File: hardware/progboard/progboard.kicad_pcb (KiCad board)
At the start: 2 copper layers, 74.9 x 58.4 mm, 37 parts, among them J1 LEFT, J2 RIGHT, J3 SWD, J4 CV A, J5 POWER

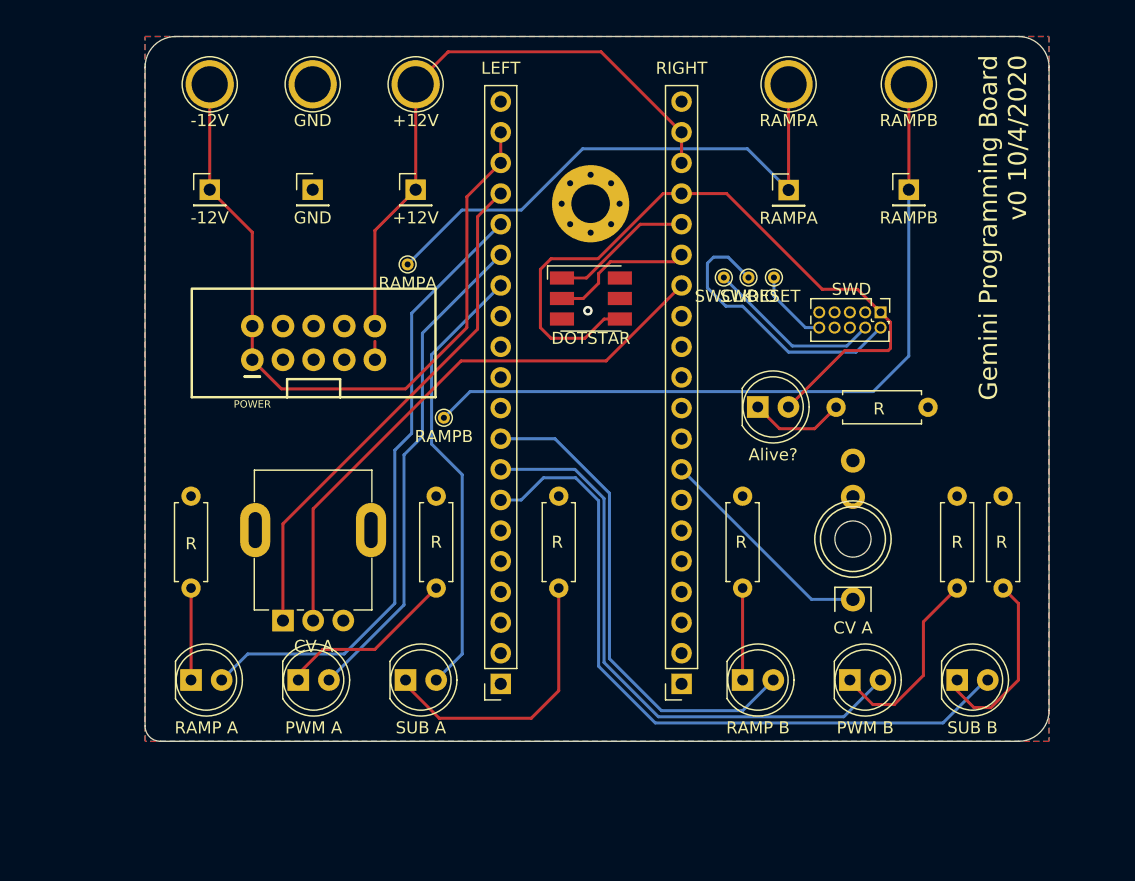
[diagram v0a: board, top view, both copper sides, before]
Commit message: Adjust drill sizes for pogo pins
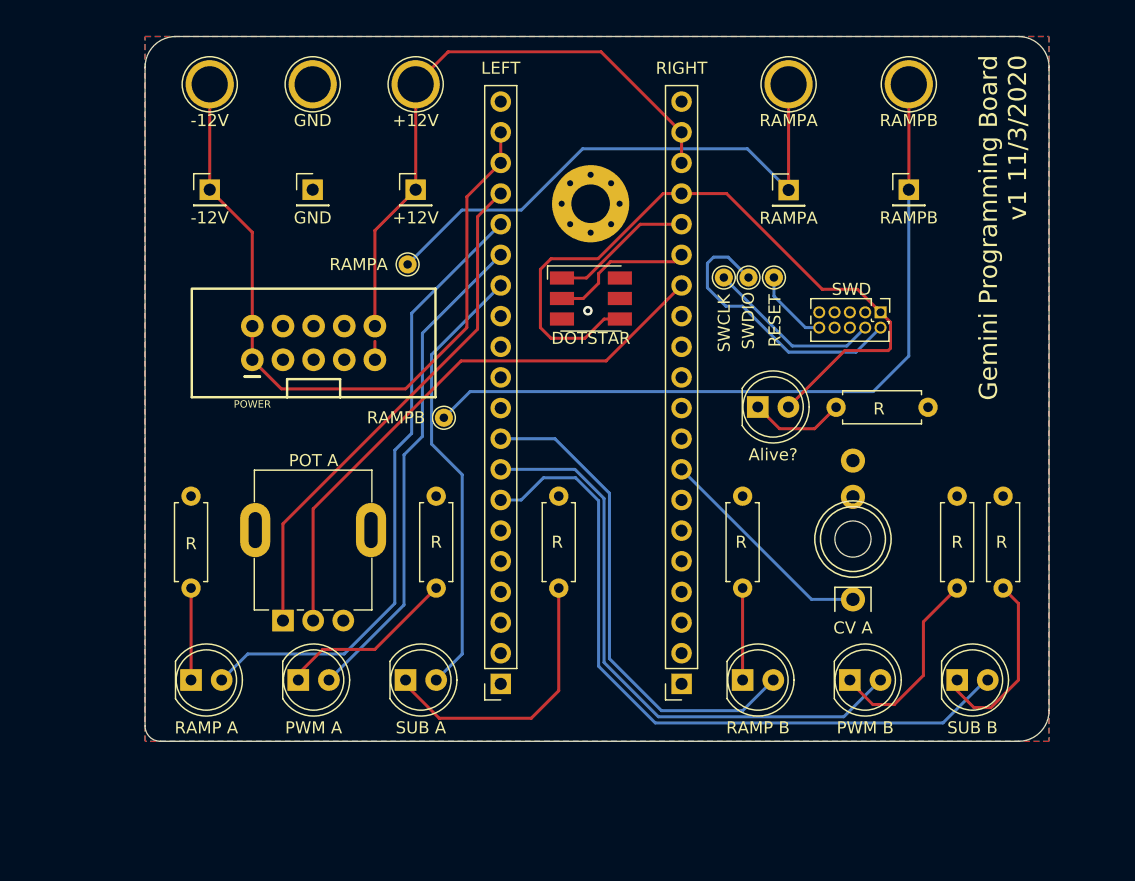
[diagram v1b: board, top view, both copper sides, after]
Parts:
- RV1: value CV A -> POT A
- TP1, TP2, TP3, TP4, TP5: footprint TestPoint:TestPoint_THTPad_D1.0mm_Drill0.5mm -> TestPoint:TestPoint_THTPad_D1.5mm_Drill0.7mm
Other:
- board text added: "Gemini Programming Board v1 11/3/2020"
- board text removed: "Gemini Programming Board v0 10/4/2020"

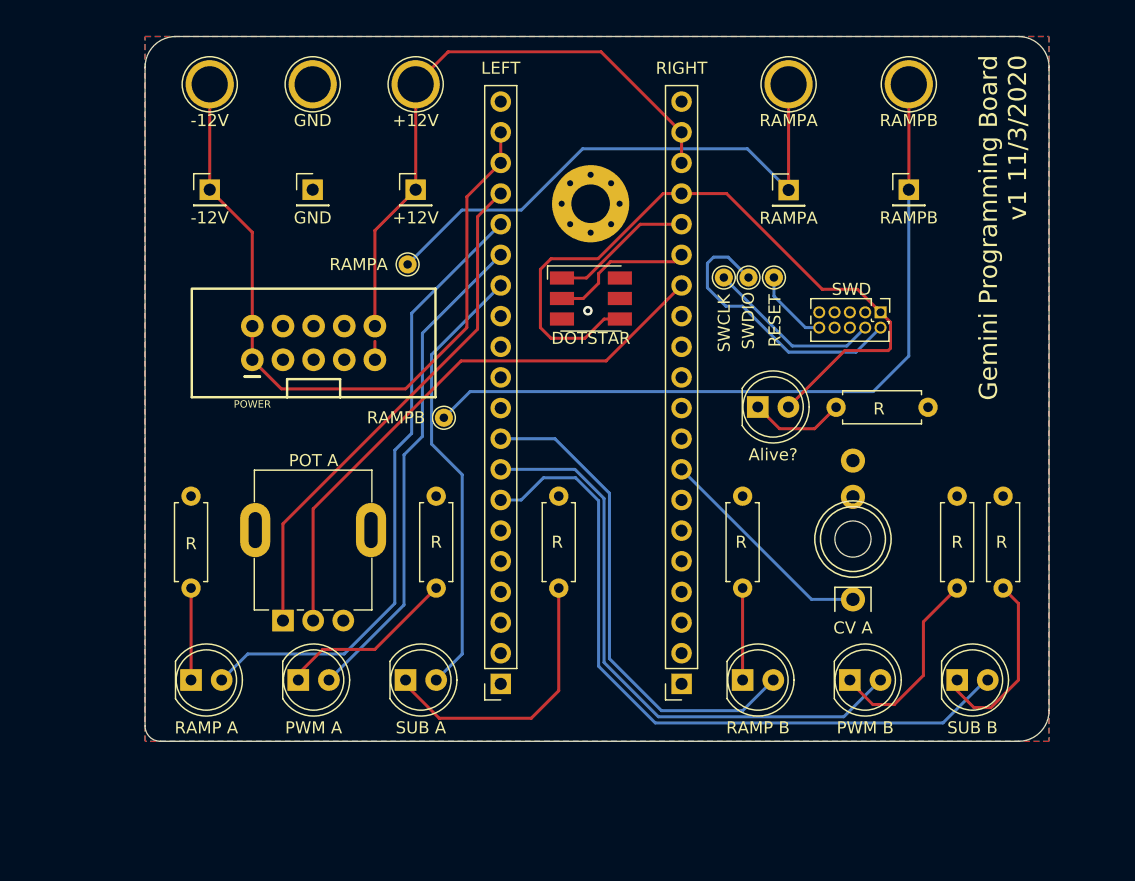
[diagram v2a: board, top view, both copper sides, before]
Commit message: hardware: new revision of programming board with more comprehensive test points
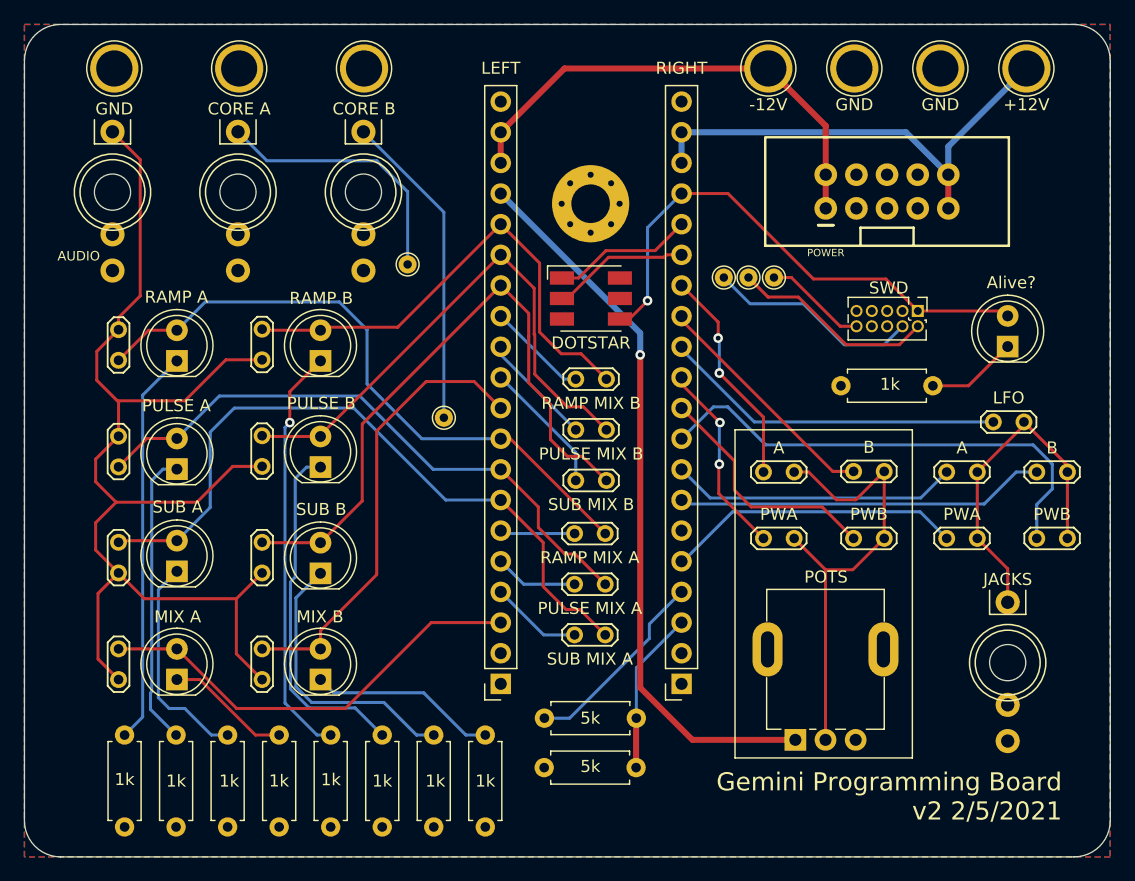
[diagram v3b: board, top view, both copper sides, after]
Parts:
- removed TP11: -12V, Connector_PinHeader_2.54mm:PinHeader_1x01_P2.54mm_Vertical
- removed TP12: GND, Connector_PinHeader_2.54mm:PinHeader_1x01_P2.54mm_Vertical
- removed TP13: +12V, Connector_PinHeader_2.54mm:PinHeader_1x01_P2.54mm_Vertical
- removed TP14: RAMPA, Connector_PinHeader_2.54mm:PinHeader_1x01_P2.54mm_Vertical
- removed TP15: RAMPB, Connector_PinHeader_2.54mm:PinHeader_1x01_P2.54mm_Vertical
- added D10: MIX B, LED_THT:LED_D5.0mm, F.Cu at (130.1, 115.5)
- added D9: MIX A, LED_THT:LED_D5.0mm, F.Cu at (118.2, 115.5)
- added J6: AUDIO, progboard:WQP-PJ301M-12_JACK, F.Cu at (112.9, 75.1)
- added J7: CORE A, progboard:WQP-PJ301M-12_JACK, F.Cu at (123.3, 75.1)
- added J8: CORE B, progboard:WQP-PJ301M-12_JACK, F.Cu at (133.7, 75.1)
- added JP1: RAMP MIX A, TestPoint:TestPoint_2Pads_Pitch2.54mm_Drill0.8mm, F.Cu at (151.2, 103.4)
- added JP10: PWB, TestPoint:TestPoint_2Pads_Pitch2.54mm_Drill0.8mm, F.Cu at (176.8, 103.8)
- added JP11: RAMP A, TestPoint:TestPoint_2Pads_Pitch2.54mm_Drill0.8mm, F.Cu at (113.4, 86.5)
- added JP12: PULSE A, TestPoint:TestPoint_2Pads_Pitch2.54mm_Drill0.8mm, F.Cu at (113.4, 95.4)
- added JP13: SUB A, TestPoint:TestPoint_2Pads_Pitch2.54mm_Drill0.8mm, F.Cu at (113.4, 106.7)
- added JP14: MIX A, TestPoint:TestPoint_2Pads_Pitch2.54mm_Drill0.8mm, F.Cu at (113.4, 115.5)
- added JP15: RAMP B, TestPoint:TestPoint_2Pads_Pitch2.54mm_Drill0.8mm, F.Cu at (125.3, 89.0)
- added JP16: PULSE B, TestPoint:TestPoint_2Pads_Pitch2.54mm_Drill0.8mm, F.Cu at (125.3, 97.9)
- added JP17: SUB B, TestPoint:TestPoint_2Pads_Pitch2.54mm_Drill0.8mm, F.Cu at (125.3, 106.7)
- added JP18: MIX B, TestPoint:TestPoint_2Pads_Pitch2.54mm_Drill0.8mm, F.Cu at (125.3, 115.5)
- added JP19: A, TestPoint:TestPoint_2Pads_Pitch2.54mm_Drill0.8mm, F.Cu at (184.6, 98.3)
- added JP2: PULSE MIX A, TestPoint:TestPoint_2Pads_Pitch2.54mm_Drill0.8mm, F.Cu at (151.2, 107.6)
- added JP20: B, TestPoint:TestPoint_2Pads_Pitch2.54mm_Drill0.8mm, F.Cu at (192.0, 98.3)
- added JP21: PWA, TestPoint:TestPoint_2Pads_Pitch2.54mm_Drill0.8mm, F.Cu at (184.6, 103.8)
- added JP22: PWB, TestPoint:TestPoint_2Pads_Pitch2.54mm_Drill0.8mm, F.Cu at (192.0, 103.8)
- added JP23: LFO, TestPoint:TestPoint_2Pads_Pitch2.54mm_Drill0.8mm, F.Cu at (188.4, 94.2)
- added JP3: SUB MIX A, TestPoint:TestPoint_2Pads_Pitch2.54mm_Drill0.8mm, F.Cu at (151.2, 111.8)
- added JP4: RAMP MIX B, TestPoint:TestPoint_2Pads_Pitch2.54mm_Drill0.8mm, F.Cu at (151.3, 90.6)
- added JP5: PULSE MIX B, TestPoint:TestPoint_2Pads_Pitch2.54mm_Drill0.8mm, F.Cu at (151.3, 94.8)
- added JP6: SUB MIX B, TestPoint:TestPoint_2Pads_Pitch2.54mm_Drill0.8mm, F.Cu at (151.3, 99.0)
- added JP7: A, TestPoint:TestPoint_2Pads_Pitch2.54mm_Drill0.8mm, F.Cu at (169.4, 98.3)
- added JP8: B, TestPoint:TestPoint_2Pads_Pitch2.54mm_Drill0.8mm, F.Cu at (176.8, 98.3)
- added JP9: PWA, TestPoint:TestPoint_2Pads_Pitch2.54mm_Drill0.8mm, F.Cu at (169.4, 103.8)
- added R1: 5k, Resistor_THT:R_Axial_DIN0207_L6.3mm_D2.5mm_P7.62mm_Horizontal, F.Cu at (148.7, 118.7)
- added R11: 1k, Resistor_THT:R_Axial_DIN0207_L6.3mm_D2.5mm_P7.62mm_Horizontal, F.Cu at (143.8, 120.1)
- added R2: 5k, Resistor_THT:R_Axial_DIN0207_L6.3mm_D2.5mm_P7.62mm_Horizontal, F.Cu at (156.3, 122.8)
- added R7: 1k, Resistor_THT:R_Axial_DIN0207_L6.3mm_D2.5mm_P7.62mm_Horizontal, F.Cu at (126.7, 120.1)
- added TP16: GND, TestPoint:TestPoint_Plated_Hole_D3.0mm, F.Cu at (113.0, 64.9)
- added TP17: GND, TestPoint:TestPoint_Plated_Hole_D3.0mm, F.Cu at (181.5, 64.9)
- D3: value PWM A -> PULSE A
- D6: value PWM B -> PULSE B
- J4: value CV A -> JACKS
- R10: renamed from 1k6; value R -> 1k
- R3: renamed from 1k7; value R -> 1k
- R4: renamed from 1k1; value R -> 1k
- R5: renamed from 1k2; value R -> 1k
- R6: renamed from 1k3; value R -> 1k
- R8: renamed from 1k4; value R -> 1k
- R9: renamed from 1k5; value R -> 1k
- RV1: value POT A -> POTS
- TP10, TP5: value RAMPB -> CORE B
- TP4, TP9: value RAMPA -> CORE A
- moved D7 53.5 mm to (130.1, 106.7), turned to 90 degrees
- moved TP8 50.6 mm to (188.6, 64.9)
- moved R9 49.2 mm to (135.2, 120.1), turned to 270 degrees
- moved J5 49.2 mm to (177.1, 75.1)
- moved R10 48.7 mm to (139.5, 120.1), turned to 270 degrees
- moved D6 47.3 mm to (130.1, 97.9), turned to 90 degrees
- moved TP6 46.3 mm to (167.2, 64.9)
- moved TP9 45.6 mm to (123.4, 64.9)
- moved TP10 45.2 mm to (133.7, 64.9)
- moved TP7 44.9 mm to (174.4, 64.9)
- moved D5 43.9 mm to (130.1, 89.1), turned to 90 degrees
- moved RV1 43.6 mm to (169.5, 120.5)
- moved R8 36.3 mm to (131.0, 120.1), turned to 270 degrees
- moved R6 30.0 mm to (122.4, 120.1), turned to 270 degrees
- moved D2 26.5 mm to (118.2, 89.1), turned to 90 degrees
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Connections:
- net Net-(J2-Pad2) renamed /mix_out
- net Net-(J2-Pad6) renamed /button
- D2 pad 2: /pollux_ramp -> /castor_ramp
- D3 pad 2: /pollux_pwm -> /castor_pwm
- D4 pad 2: /pollux_sub -> /castor_sub
- D5 pad 2: /castor_ramp -> /pollux_ramp
- D6 pad 2: /castor_pwm -> /pollux_pwm
- D7 pad 2: /castor_sub -> /pollux_sub
- J1 pad 10: Net-(J1-Pad10) -> /pollux_mix_out
- J1 pad 11: Net-(J1-Pad11) -> /pollux_sub_mix_in
- J1 pad 12: Net-(J1-Pad12) -> /pollux_pwm_mix_in
- J1 pad 13: Net-(J1-Pad13) -> /pollux_ramp_mix_in
- J1 pad 3: Net-(J1-Pad3) -> /castor_mix_out
- J1 pad 4: Net-(J1-Pad4) -> /castor_sub_mix_in
- J1 pad 5: Net-(J1-Pad5) -> /castor_pwm_mix_in
- J1 pad 6: Net-(J1-Pad6) -> /castor_ramp_mix_in
- J2 pad 10: Net-(J2-Pad10) -> /duty_b_pot
- J2 pad 11: Net-(J2-Pad11) -> /duty_a_pot
- J2 pad 12: Net-(J2-Pad12) -> /chorus_pot
- J2 pad 13: Net-(J2-Pad13) -> /cv_b_pot
- J2 pad 3: Net-(J2-Pad3) -> /mix_pot_in
- J2 pad 4: Net-(J2-Pad4) -> /mix_pot_out
- J2 pad 5: Net-(J2-Pad5) -> /duty_a_jack
- J2 pad 7: Net-(J2-Pad7) -> /cv_b_jack
- J2 pad 9: Net-(J2-Pad9) -> /duty_b_jack
- J4 pad T: /cv_a_jack -> Net-(J4-PadT)
- J5 pad 9: Net-(J5-Pad9) -> +12V
- RV1 pad 2: /cv_a_pot -> Net-(JP10-Pad1)
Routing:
- net Net-(J6-PadT): track 0.00 -> 101.0 mm
- net /duty_b_jack: track 0.00 -> 40.5 mm
- net Net-(JP10-Pad1): track 0.00 -> 38.7 mm
- net /pollux_mix_out: track 0.00 -> 37.7 mm
- net Net-(J8-PadT): track 63.2 -> 26.5 mm
- net /castor_mix_out: track 0.00 -> 36.7 mm
- net /cv_b_jack: track 0.00 -> 30.7 mm
- net /cv_a_pot: track 47.5 -> 18.3 mm, vias 0 -> 2
- net Net-(J4-PadT): track 0.00 -> 28.7 mm
- net /chorus_pot: track 0.00 -> 28.5 mm
- net Net-(D5-Pad1): track 7.62 -> 34.5 mm, vias 0 -> 1
- net Net-(D2-Pad1): track 7.62 -> 32.8 mm
- net /duty_a_jack: track 0.00 -> 24.6 mm
- net Net-(J7-PadT): track 45.7 -> 22.1 mm
- net -12V: track 62.5 -> 40.5 mm
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- added copper zone on B.Cu, net /pollux_sub
- removed copper zone on B.Cu, net GND
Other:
- board size 74.9 x 58.4 mm -> 90 x 69 mm
- board text added: "Gemini Programming Board v2 2/5/2021"
- board text removed: "Gemini Programming Board v1 11/3/2020"
- board text removed: "OwO"

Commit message: hardware/progboard: Add dedicated jack for interfacing with knob inputs
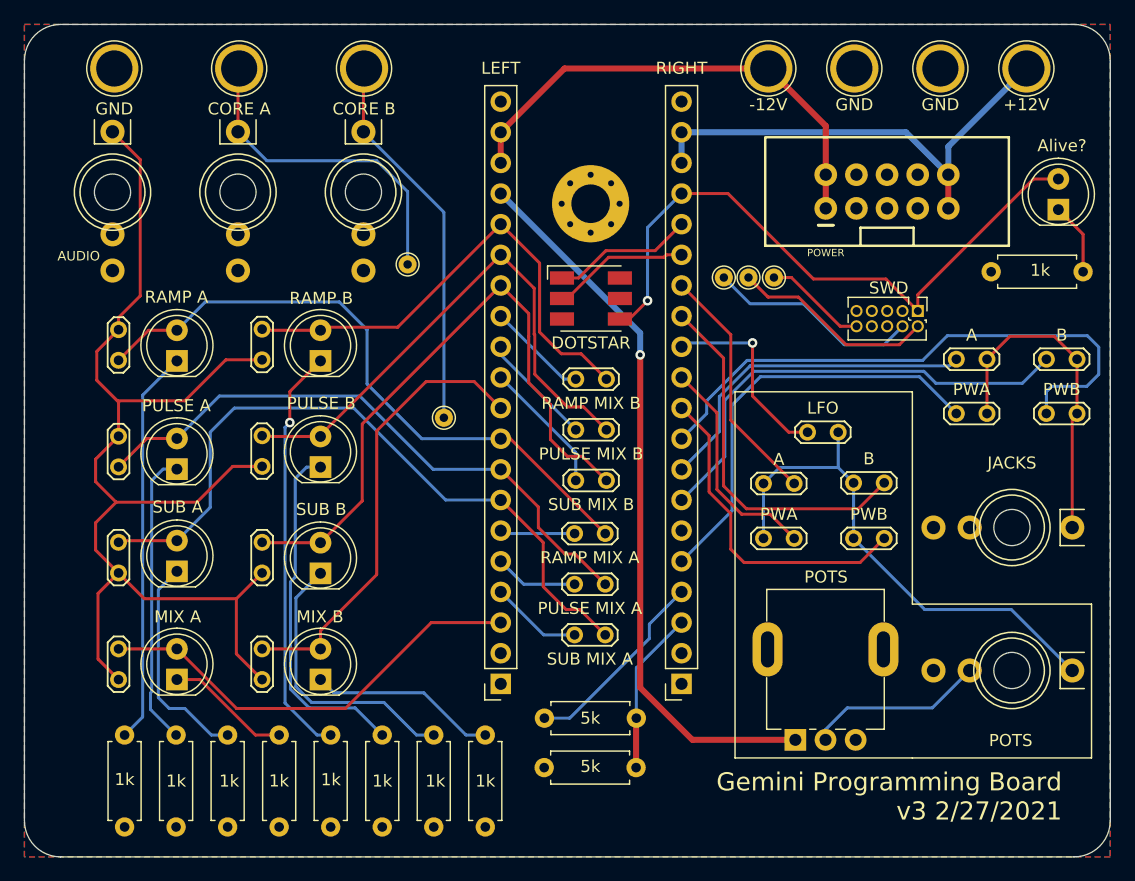
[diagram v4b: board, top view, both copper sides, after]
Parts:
- added J9: POTS, progboard:WQP-PJ301M-12_JACK, F.Cu at (187.4, 114.8)
- moved R3 15.6 mm to (193.3, 81.7)
- moved JP23 15.4 mm to (173.0, 95.0)
- moved D8 12.1 mm to (191.3, 76.6)
- moved J4 11.2 mm to (187.4, 102.9), turned to 270 degrees
- moved JP21 10.4 mm to (185.4, 93.5)
- moved JP22 10.4 mm to (192.8, 93.5)
- moved JP19 9.38 mm to (185.4, 89.0)
- moved JP20 9.38 mm to (192.8, 89.0)
- moved JP7 0.95 mm to (169.4, 99.3)
- moved JP8 0.95 mm to (176.8, 99.2)
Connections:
- JP10 pad 1: Net-(JP10-Pad1) -> /duty_b_pot
- JP10 pad 2: /duty_b_pot -> Net-(J9-PadT)
- JP23 pad 1: Net-(J4-PadT) -> Net-(J9-PadT)
- JP7 pad 1: Net-(JP10-Pad1) -> /cv_a_pot
- JP7 pad 2: /cv_a_pot -> Net-(J9-PadT)
- JP8 pad 1: Net-(JP10-Pad1) -> /cv_b_pot
- JP8 pad 2: /cv_b_pot -> Net-(J9-PadT)
- JP9 pad 1: Net-(JP10-Pad1) -> /duty_a_pot
- JP9 pad 2: /duty_a_pot -> Net-(J9-PadT)
- RV1 pad 2: Net-(JP10-Pad1) -> Net-(J9-PadTN)
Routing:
- net Net-(J9-PadT): track 0.00 -> 43.3 mm
- net Net-(JP10-Pad1): track 38.7 -> 0.00 mm
- net Net-(J9-PadTN): track 0.00 -> 14.8 mm
- net /chorus_pot: track 28.5 -> 16.2 mm, vias 0 -> 1
- net /duty_a_jack: track 24.6 -> 35.5 mm
- net /cv_b_pot: track 19.8 -> 30.5 mm
- net +3V3: track 44.2 -> 53.6 mm
- net /cv_b_jack: track 30.7 -> 38.6 mm
- net /duty_b_jack: track 40.5 -> 48.1 mm
- net /duty_b_pot: track 20.2 -> 27.4 mm
- net Net-(J7-PadT): track 22.1 -> 27.4 mm
- net Net-(J8-PadT): track 26.5 -> 31.7 mm
- net /cv_a_jack: track 23.8 -> 28.3 mm
- net /duty_a_pot: track 16.2 -> 18.6 mm, vias 2 -> 0
- net /cv_a_pot: track 18.3 -> 20.3 mm, vias 2 -> 0
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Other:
- board text added: "Gemini Programming Board v3 2/27/2021"
- board text removed: "Gemini Programming Board v2 2/5/2021"
